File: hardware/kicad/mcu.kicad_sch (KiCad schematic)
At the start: 6 parts, among them J2 SWD/UART Recovery (DNP), U3 ESP32-C6-DevKitM-1-N4

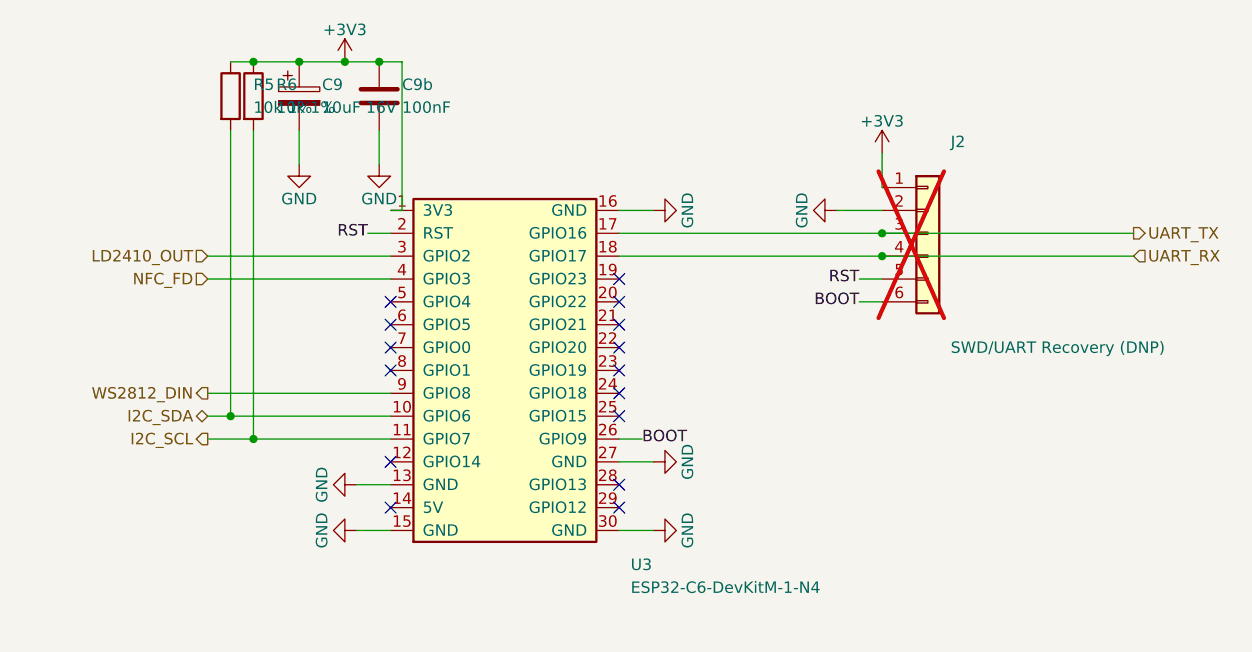
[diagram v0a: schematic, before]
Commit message: kicad+docs: v0.19 - IO sub-sheet populated (J9 Qwiic + J10 native-USB recovery DNP)
Closes review Mi4 ("IO sub-sheet still empty"). Implements both connectors
listed in CLAUDE.md as "tentative" since v0.1:

J9 - Qwiic / Stemma QT expansion (always populated)
  Stock JST_SH SM04B-SRSS-TB 4-pin horizontal SMD socket on cutout C5.
  Cable mouth faces the chord so the cable plugs in from outside the
  case. Pinout: GND / +3.3V / SDA / SCL — taps the shared I2C bus
  (SEN66 + NT3H1101 + Qwiic chain). I2C_SDA / I2C_SCL hier labels
  match the MCU exports.

J10 - Native-USB recovery header (DNP)
  Stock 6-pin 2.54 mm vertical THT pin header on cutout C3. Pads
  only — solder a header for emergency reflashing if both DevKitM-1
  on-module USB-C ports are damaged. Pinout (chord side → PCB
  interior): GND / +3V3 / USB_DM (GPIO 12) / USB_DP (GPIO 13) /
  EN (chip reset) / BOOT (GPIO 9 strap).

Cutout C4 reserved as v2 expansion placeholder (no connector).

Key plumbing changes:
  - GPIO 12 / GPIO 13 moved from ESP32C6_DEVKITM1_NC_PINS to
    ESP32C6_DEVKITM1_SIGNAL_PIN as USB_DM / USB_DP. MCU sheet now
    wires U3.28 / U3.29 east to hier labels.
  - EN / BOOT migrated from MCU sub-sheet local labels to hier
    labels so the same nets reach the IO sheet's J10.5 / J10.6.
    J2_PIN_MAP[5] "RST" -> "EN".
  - CUTOUTS extended with allow_pads bool; C3 and C5 flip the
    copper keepout zone's pads-not-allowed rule so connector pads
    can live inside the case-wall opening.
  - SUBSHEET_SIZE bumped to (38.1, 17.78) for 6 pins per edge.
  - Root sheet inter-sheet wires extended for I2C bus → IO + new
    routes for USB_DM/USB_DP/EN/BOOT (MCU right ↔ IO left).
  - _emit_stock_lib_footprint() factored out the parse-and-patch
    logic shared by gen_j1/j3/j4 footprint generators; gen_j9 and
    gen_j10 are thin wrappers around it.

DRC = 0, ERC = 0.

BOM impact: +1 SKU (JST SM04B-SRSS-TB, ~€0.50). J10 pin header is
DNP — 0 BOM lines for the production assembly.

Co-Authored-By: Clau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
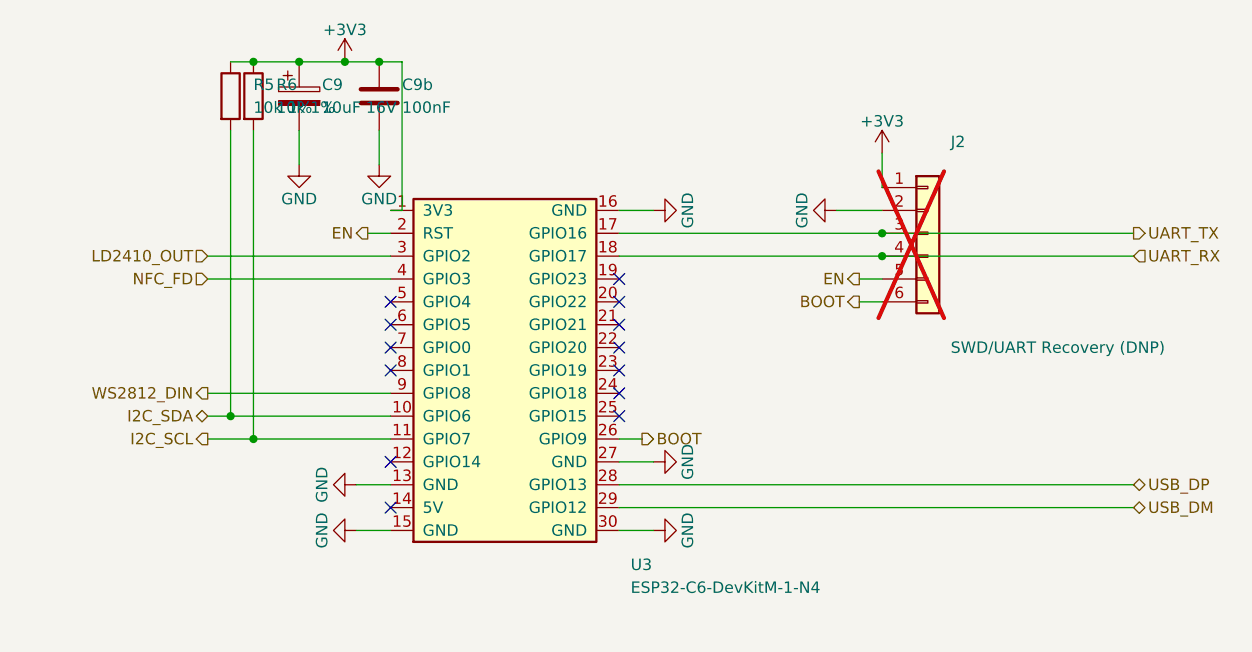
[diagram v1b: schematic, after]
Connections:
- net USB_DP: now reaches U3.28 (GPIO13)
- net USB_DM: now reaches U3.29 (GPIO12)
- net RST renamed EN
- no-connect marks 15 -> 13
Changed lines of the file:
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@@
 	)
 )
-(label "RST"
+(hierarchical_label "EN"
+	(shape output)
 	(at 137.16 95.25 180)
 	(effects
@@
 	)
 )
-(label "BOOT"
+(hierarchical_label "BOOT"
+	(shape output)
 	(at 167.64 118.11 0)
 	(effects
@@
 (wire
 	(pts
+		(xy 165.1 123.19) (xy 222.25 123.19)
+	)
+	(stroke
+		(width 0)
+		(type default)
+	)
+)
+(hierarchical_label "USB_DP"
+	(shape bidirectional)
+	(at 222.25 123.19 0)
+	(effects
+		(font
+			(size 1.27 1.27)
+		)
+		(justify left)
+	)
+)
+(wire
+	(pts
+		(xy 165.1 125.73) (xy 222.25 125.73)
+	)
+	(stroke
+		(width 0)
+		(type default)
+	)
+)
+(hierarchical_label "USB_DM"
+	(shape bidirectional)
+	(at 222.25 125.73 0)
+	(effects
+		(font
+			(size 1.27 1.27)
+		)
+		(justify left)
+	)
+)
+(wire
+	(pts
 		(xy 194.31 100.33) (xy 191.77 100.33)
 	)
@@
 	)
 )
-(label "RST"
+(hierarchical_label "EN"
+	(shape output)
 	(at 191.77 100.33 180)
 	(effects
@@
 	)
 )
-(label "BOOT"
+(hierarchical_label "BOOT"
+	(shape output)
 	(at 191.77 102.87 180)
 	(effects
@@
 	(at 165.1 115.57)
 )
-(no_connect
-	(at 165.1 123.19)
-)
-(no_connect
-	(at 165.1 125.73)
-)
         	(symbol

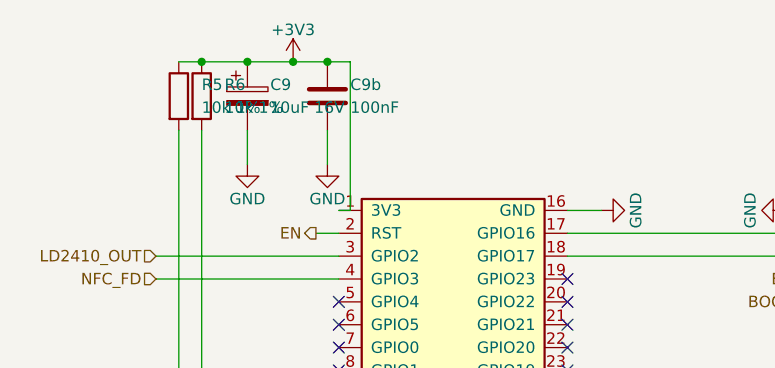
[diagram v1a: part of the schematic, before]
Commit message: kicad: v0.20 - C3 renumber HF-bypass caps C3b/C4b/C5b/C6b/C9b -> C13..C17
Pre-routing review v0.19 finding C3 (Critical): KiCad's BOM annotator
treats trailing-letter references like 'C3b' as un-annotated 'C3' + suffix
letter, emitting them as 'C3b?' on BOM export and breaking JLCPCB / Mouser
upload. Renamed in lockstep across schematic / wire labels / Python local
identifiers (no electrical change):

  C3b -> C13   (input HF bypass at U1.VIN)
  C4b -> C14   (output HF bypass at +5V)
  C5b -> C15   (input HF bypass at U2.VIN)
  C6b -> C16   (output HF bypass at +3V3)
  C9b -> C17   (HF decoupling at ESP32 +3V3)

ERC=0, DRC=0. BOM export verified: all five caps now appear as plain
"C13".."C17" with no '?' suffix.

Co-Authored-By: Claude Opus 4.7 (1M context) <noreply@anthropic.com>
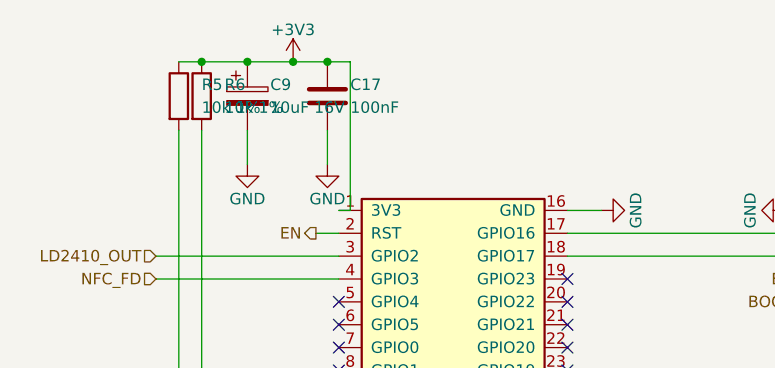
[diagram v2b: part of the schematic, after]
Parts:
- removed C9b: 100nF, symbol Device:C
- added C17: 100nF, symbol Device:C
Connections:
- net +3V3: now also C17.1
- net GND: now also C17.2
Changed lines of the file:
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@@
 	(dnp no)
 	(fields_autoplaced yes)
-	(property "Reference" "C9b"
+	(property "Reference" "C17"
 		(at 140.97 78.74 0)
 		(effects
@@
 		(project "oas"
 			(path "/515343fe-5590-5fd9-97ec-5bed0f979de2/5a2a7aae-0596-52cb-bb07-90c47115320c"
-				(reference "C9b")
+				(reference "C17")
 				(unit 1)
 			)

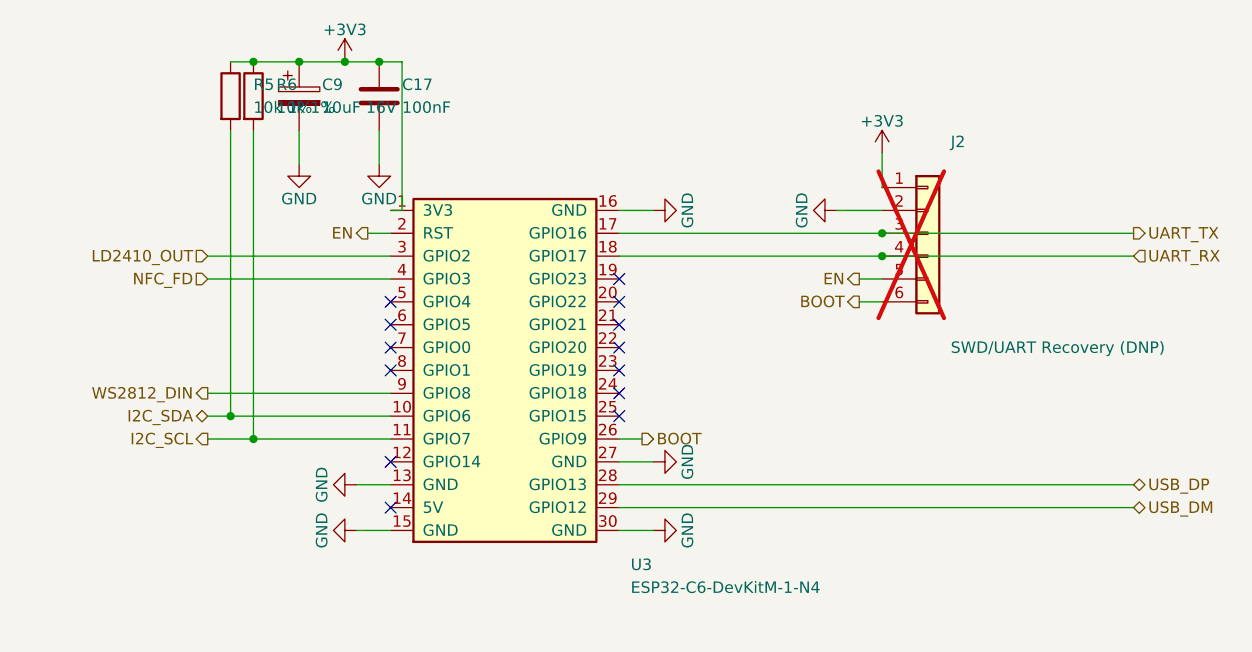
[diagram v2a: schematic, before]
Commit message: kicad+docs: v0.21 - M3 closure (J5/J6/J7/J8 schematic) + UART/USB crossover fix
M3 part 1 (MCU): replace U3 placeholder with J5 + J6 schematic symbols
(Conn_01x15 each). J5 = ESP32 J1 antenna-side row (pin tips left,
angle=0); J6 = ESP32 J3 USB-side row (pin tips right, angle=180). Pin
numbers 1..15 match PCB pad numbering 1:1. All 7 OAS signal pins get
hier-label stubs; 5 GND pins get power flags; 13 NC pins get
no_connect markers. J2 DNP recovery header rotated 180 so its TX/RX
pin row aligns with J6 UART_TX/RX.

M3 part 2 (Sensors): replace U4 mikroBUS placeholder with J7 + J8
schematic symbols (Conn_01x08 each). J7 = mikroBUS pins 1..8 (LEFT
column, angle=0); J8 = mikroBUS pins 9..16 (RIGHT column, angle=180).
J7 pin 7 = +3V3, J7 pin 8 = GND, J8 pin 2 = NFC_FD, J8 pin 5 = SCL,
J8 pin 6 = SDA, J8 pin 8 = GND; 10 unused pins get no_connect markers.

Root-sheet UART/USB crossover bug fixed (pre-existing v0.20 finding):
the UART_TX east-from-sensors wire ran at Y=97.79 in the same column
as the IO sub-sheet's USB_DP west-into-io wire (also at Y=97.79),
overlapping in X range [101.6, 143.51] and bridging UART_TX into
USB_DP. Same pattern for UART_RX/EN at Y=100.33. Fix re-routes UART
east stubs south of the IO block before going east (Y=110.49 for
UART_TX, Y=113.03 for UART_RX), eliminating the Y collision. Verified
clean: /MCU/UART_TX = {J2.3, J4.3, J6.2}, /MCU/UART_RX = {J2.4, J4.2,
J6.3}, /IO/USB_DP / EN no longer contain LD2410 or UART pins.

SEN66 mech-ref F.CrtYd removed (5 of 15 v0.20 DRC violations were
false-positive courtyards_overlap between SENS1 body and PCB-surface
SMD parts; SEN66 floats 21.5 mm above PCB so the 2D courtyard rule
doesn't reflect physical clearance). Matches the existing convention
in _emit_daughterboard_reference_pcb_footprint() (MOD1/MOD2).

Net coverage: 216 pad-net assignments applied by
sync_pcb_nets_from_schematic (up from 188 in v0.20). All J5..J8
sockets fully assigned. DRC: 10 violations (down from 15) - 1
courtyards_overlap C4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
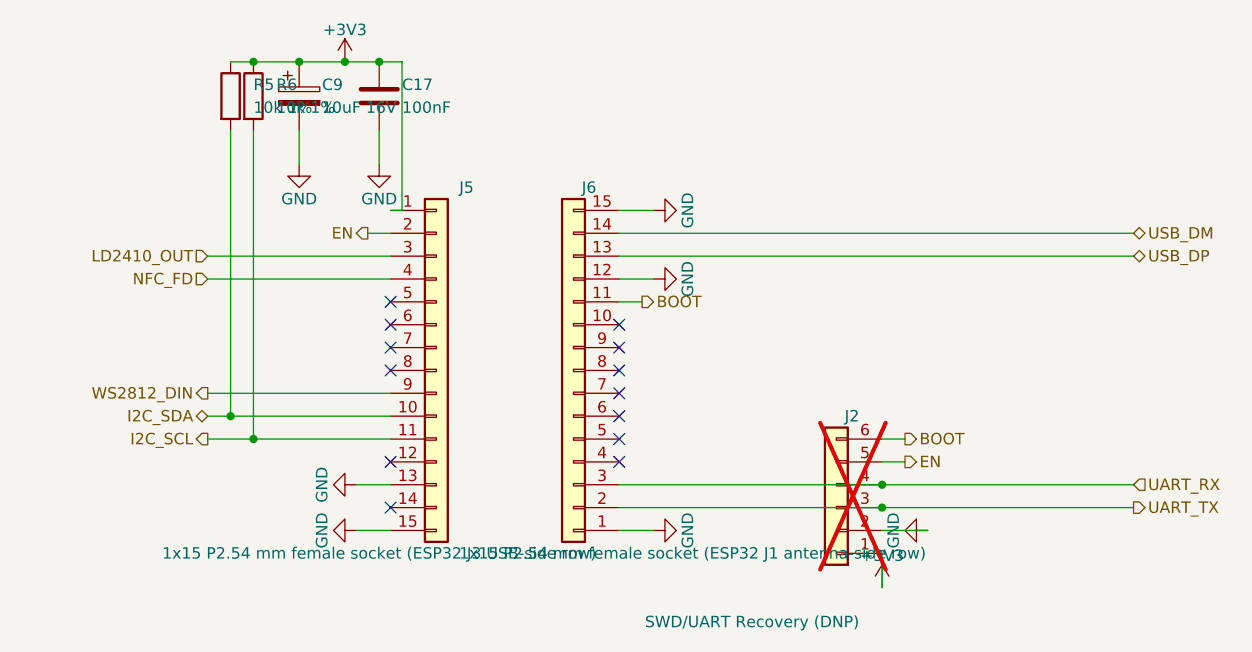
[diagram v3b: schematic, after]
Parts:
- removed U3: ESP32-C6-DevKitM-1-N4, symbol OAS:ESP32-C6_DevKitM-1
- added J5: 1x15 P2.54 mm female socket (ESP32 J1 antenna-sid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, symbol Connector_Generic:Conn_01x15
- added J6: 1x15 P2.54 mm female socket (ESP32 J3 USB-side ro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, symbol Connector_Generic:Conn_01x15
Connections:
- net +3V3: now also J5.1 (Pin_1)
- net BOOT: now also J6.11 (Pin_11)
- net EN: now also J5.2 (Pin_2)
- net GND: now also J5.13 (Pin_13), J5.15 (Pin_15), J6.1 (Pin_1), J6.12 (Pin_12), J6.15 (Pin_15)
- net I2C_SCL: now also J5.11 (Pin_11)
- net I2C_SDA: now also J5.10 (Pin_10)
- net LD2410_OUT: now also J5.3 (Pin_3)
- net NFC_FD: now also J5.4 (Pin_4)
- net UART_RX: now also J6.3 (Pin_3)
- net UART_TX: now also J6.2 (Pin_2)
- net USB_DM: now also J6.14 (Pin_14)
- net USB_DP: now also J6.13 (Pin_13)
- net WS2812_DIN: now also J5.9 (Pin_9)
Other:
- moved on the sheet: J2

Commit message: kicad: v0.22 - restore SEN66 courtyard guardrail + relocate offending SMD
The v0.21 changelog removed the SEN66 mech-ref F.CrtYd rectangle on the
reasoning that "SEN66 sits 21.5 mm above the OAS PCB". THIS WAS WRONG.
The SEN66 lies FLAT on the PCB on its 25.6 x 55.2 mm back face - the
21.5 mm is body height ABOVE the PCB, not standoff. SMD components in
the SEN66 body shadow would be physically crushed.

v0.22 restores the F.CrtYd as a programmatic DRC guardrail (any future
SMD placed under SEN66 triggers courtyards_overlap), and relocates the
5 currently-conflicting parts (Q1, F1, D3, R1, R4) to the strips north
and far-east of SEN66. Also fixes 13 NFC + ESP32 partial-overlap parts
via a clean column-based layout fully inside the ESP32 daughterboard
body shadow.

Additional v0.22 fixes:
- Task #24: Q1 SOT-23 pad names "G"/"S"/"D" matching Device:Q_PMOS so
  netlist sync binds Q1 pads (were on no_net previously).
- Task #17 M1: I2C pull-ups R5/R6 reverted 10k -> 4.7k for rise-time
  margin at the realized ~220 mm total bus length (PCB MST + cable).
- Task #18 M2: new R7 = 10k GPIO 8 boot-strap pull-up to +3V3,
  replacing the disappeared DevKitM-1 onboard pull-up (VCC_5V floats).
- M5 doc fix: CLAUDE.md "Shared I2C bus" updated with honest cable
  length measurement (~140 mm PCB MST + ~80 mm cable = ~220 mm).
- DRC silk_over_copper residue cleared by moving the ESP32 daughterboard
  body labels to F.Fab (assembly-drawing-only); C11 LD2410 decoupling
  cap shifted +2 mm east to clear LDR1 mech-ref silk-frame long edge.

DRC = 0 errors/warnings, ERC = 0, 160 unconnected pads (expected
pre-routing ratlines).

Co-Authored-By: Claude Opus 4.7 (1M context) <noreply@anthropic.com>
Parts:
- added R7: 10k 1%, symbol Device:R
- R5, R6: value 10k 1% -> 4.7k 1%
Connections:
- net +3V3: now also R7.1
- net WS2812_DIN: now also R7.2
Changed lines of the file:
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@@
+(wire
+	(pts
+		(xy 152.4 83.82) (xy 152.4 76.2)
+	)
+	(stroke
+		(width 0)
+		(type default)
+	)
+)
+(wire
+	(pts
+		(xy 140.97 76.2) (xy 152.4 76.2)
+	)
+	(stroke
+		(width 0)
+		(type default)
+	)
+)
+(junction
+	(at 140.97 76.2)
+	(diameter 0)
+	(color 0 0 0 0)
+)
+(wire
+	(pts
+		(xy 152.4 91.44) (xy 152.4 113.03)
+	)
+	(stroke
+		(width 0)
+		(type default)
+	)
+)
+(wire
+	(pts
+		(xy 139.7 113.03) (xy 152.4 113.03)
+	)
+	(stroke
+		(width 0)
+		(type default)
+	)
+)
+(junction
+	(at 152.4 113.03)
+	(diameter 0)
+	(color 0 0 0 0)
+)
 (wire
 	(pts
@@
 		)
 	)
-	(property "Value" "10k 1%"
+	(property "Value" "4.7k 1%"
 		(at 124.46 81.28 0)
 		(effects
@@
 		)
 	)
-	(property "Value" "10k 1%"
+	(property "Value" "4.7k 1%"
 		(at 127 81.28 0)
 		(effects
@@
 				(unit 1)
 			)
+		)
+	)
+)
+(symbol
+	(lib_id "Device:R")
+	(at 152.4 87.63 0)
+	(unit 1)
+	(exclude_from_sim no)
+	(in_bom yes)
+	(on_board yes)
+	(dnp no)
+	(fields_autoplaced yes)
+	(property "Reference" "R7"
+		(at 154.94 86.36 0)
+		(effects
+			(font
+				(size 1.27 1.27)
+			)
+			(justify left)
+		)
+	)
+	(property "Value" "10k 1%"
+		(at 154.94 88.9 0)
+		(effects
+			(font
+				(size 1.27 1.27)
+			)
+			(justify left)
+		)
+	)
+	(property "Footprint" ""
+		(at 152.4 87.63 90)
+		(effects
+			(font
+				(size 1.27 1.27)
+			)
+			(hide yes)
+		)
+	)
+	(property "Datasheet" ""
+		(at 152.4 87.63 0)
+		(effects
+			(font
+				(size 1.27 1.27)
+			)
+			(hide yes)
+		)
+	)
+	(property "Description" ""
+		(at 152.4 87.63 0)
+		(effects
+			(font
+				(size 1.27 1.27)
+			)
+			(hide yes)
+		)
+	)
+	(pin "1"
+	)
+	(pin "2"
+	)
+	(instances
+		(project "oas"
+			(path "/515343fe-5590-5fd9-97ec-5bed0f979de2/5a2a7aae-0596-52cb-bb07-90c47115320c"
+				(reference "R7")
+				(unit 1)
+			)

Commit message: kicad+docs: v0.24 - fix v0.23 regressions (lib-qualify footprints + ERC strict)
Closes review iteration 2 findings (`_review-iteration-2-v0.23.md`):

1. Mn3 V3 regression — lib-qualify footprint back-fill.
   `_build_pcb_ref_to_footprint()` now lib-qualifies bare PCB-side
   Footprint property values via a new `BARE_FOOTPRINT_TO_LIB` table
   (12 entries) and asserts every returned value contains `:`. In
   parallel, the inline `gen_*_pcb_footprint` generators that emitted
   bare names now write fully-qualified `Lib:Name` strings directly
   (`Capacitor_SMD:C_0402_1005Metric`, `Package_TO_SOT_SMD:SOT-23`,
   `Inductor_SMD:L_APV_ANR5040`, `Fuse:Fuse_2920_7451Metric`,
   `Capacitor_THT:CP_Radial_D8.0mm_P3.50mm`, etc.). 15 ERC
   `footprint_link_issues` warnings → 0.

2. Mj2 — `regenerate.py` ERC strict mode. `kicad-cli sch erc` now
   invoked with `--severity-error --severity-warning
   --exit-code-violations`, mirroring DRC strictness. Verified by
   corrupting a schematic Footprint property and confirming abort.
   CLAUDE.md "PCB design workflow" §3 ("aborts on any error or
   warning") is now actually enforced for ERC, not just DRC.

3. C1 V4 — derived `.kicad_pcb` / `.kicad_sch` resynced with
   `generate.py`. The v0.23 commit shipped `generate.py` updates
   without regenerating the derived files; this commit brings them
   into sync via `python regenerate.py`.

4. Mj1 — CLAUDE.md v0.23 changelog entry added retroactively
   (had been missing). v0.24 entry added documenting this fix
   series + the ERC-strictness lesson.

5. `hardware/components/_review-iteration-2-v0.23.md` committed
   (previously untracked).

DRC = 0 violations / 0 warnings.
ERC = 0 violations / 0 warnings (now strict).
Determinism self-check passes (17 files bit-identical across two
consecutive `regenerate.py` runs).

Co-Authored-By: Claude Opus 4.7 (1M context) <noreply@anthropic.com>
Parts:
- J2: footprint (none) -> Connector_PinHeader_2.54mm:PinHeader_1x06_P2.54mm_Vertical
- J5, J6: footprint (none) -> Connector_PinSocket_2.54mm:PinSocket_1x15_P2.54mm_Vertical
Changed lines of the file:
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@@
         			)
         		)
-        		(property "Footprint" ""
+        		(property "Footprint" "Connector_PinSocket_2.54mm:PinSocket_1x15_P2.54mm_Vertical"
         			(at 144.78 110.49 0)
         			(effects
@@
         			)
         		)
-        		(property "Footprint" ""
+        		(property "Footprint" "Connector_PinSocket_2.54mm:PinSocket_1x15_P2.54mm_Vertical"
         			(at 160.02 110.49 0)
         			(effects
@@
         			)
         		)
-        		(property "Footprint" ""
+        		(property "Footprint" "Connector_PinHeader_2.54mm:PinHeader_1x06_P2.54mm_Vertical"
         			(at 189.23 125.73 0)
         			(effects
